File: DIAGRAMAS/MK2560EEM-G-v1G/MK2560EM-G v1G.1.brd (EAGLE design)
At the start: 102.5 x 87.6 mm, 70 parts, among them U1 X-MOTOR, U2 Y-MOTOR, U3 Z-MOTOR

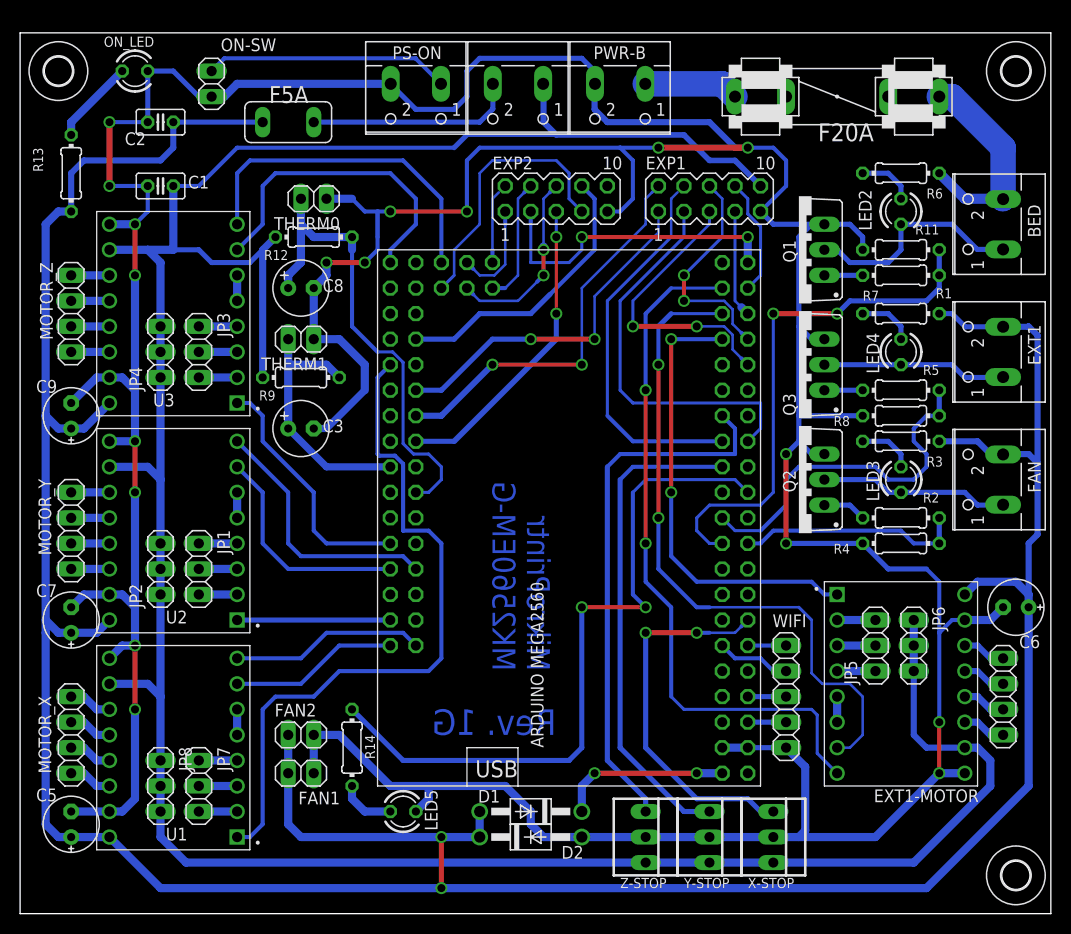
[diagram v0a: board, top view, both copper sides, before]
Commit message: pcb fixes v1G.1
- pcb bug corrections space clearance on x,y,z drivers resolution pin headers. changed for right pin headers.
- changed F5A fuse for +12v rail, for aa short cylinder standard fuse.
- pcb resized, for more space, and better alocation of components.
-
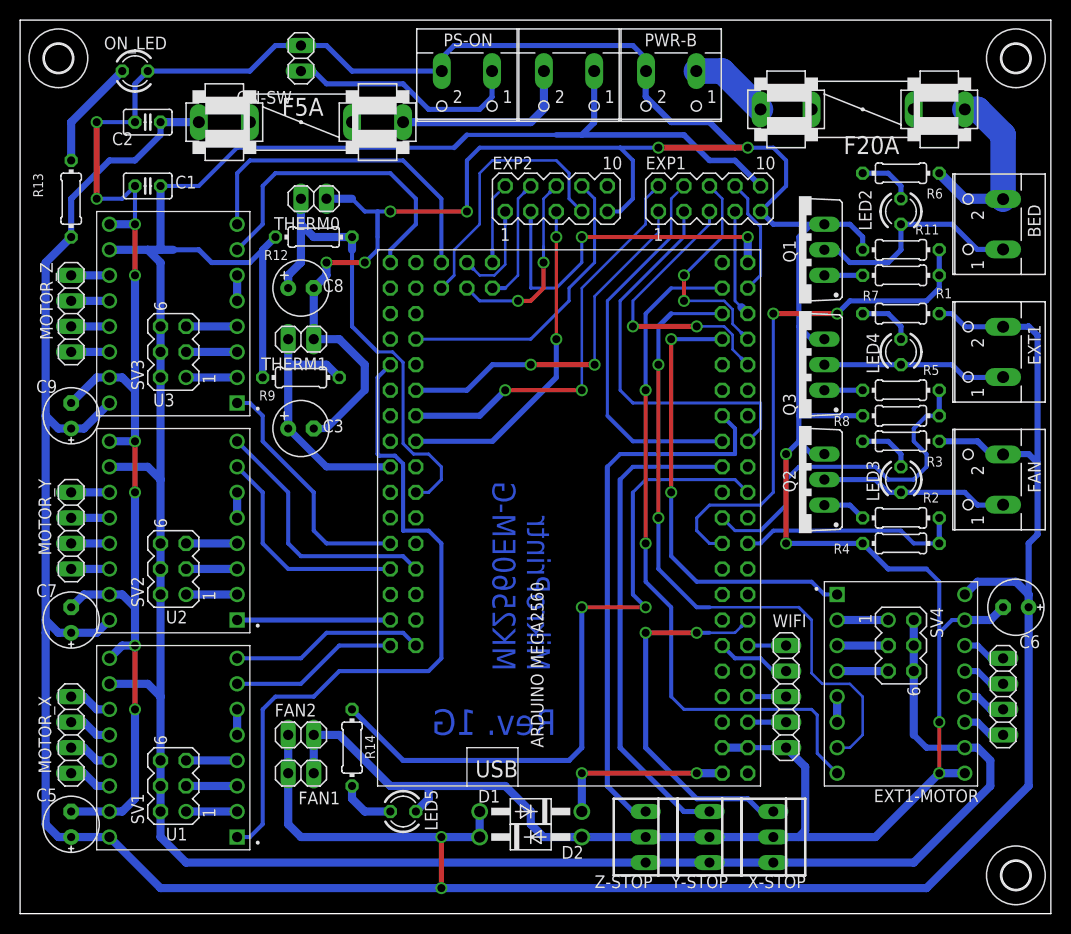
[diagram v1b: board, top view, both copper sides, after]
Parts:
- removed JP1, JP2, JP3, JP4, JP5, JP6, JP7, JP8: (no value), -redpic-connector:1X03
- added SV1, SV2, SV3, SV4: (no value), con-lstb:MA03-2
- F5A: device fuse:TE5 -> special:FUSE1
- moved ON-SW 9.25 mm to (25.4, 76.2), turned to 90 degrees
- moved +12V_+5V 5.24 mm to (52.1, 73.7)
- moved PS-ON 5.24 mm to (41.9, 73.7)
- moved PWR-B 5.24 mm to (62.2, 73.7)
- moved F20A 2.84 mm to (81.3, 71.1)
- moved R13 2.54 mm to (2.54, 62.2)
- moved C1 1.27 mm to (10.2, 63.5)
- moved C2 1.27 mm to (10.2, 69.8)
- moved F5A 1.27 mm to (25.4, 69.8)
- moved H1 1.27 mm to (1.27, 76.2)
- moved H2 1.27 mm to (96.5, 76.2)
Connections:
- net +12V5A: now also F5A.1A; no longer F5A.1
- net +5V: now also SV1.2, SV1.4, SV1.6, SV2.2, SV2.4, SV2.6, SV3.2, SV3.4, SV3.6, SV4.2, SV4.4, SV4.6; no longer JP2.1, JP2.2, JP2.3, JP4.1, JP4.2, JP4.3, JP6.1, JP6.2, JP6.3, JP8.1, JP8.2, JP8.3
- net N$10: now also SV1.3; no longer JP7.2
- net N$11: now also SV1.5; no longer JP7.1
- net N$14: now also SV2.1; no longer JP1.3
- net N$15: now also SV2.3; no longer JP1.2
- net N$16: now also SV2.5; no longer JP1.1
- net N$19: now also SV3.3, U3.3; no longer JP3.3, U3.2
- net N$21: now also SV3.1, U3.2; no longer JP3.2, U3.3
- net N$22: now also SV3.5; no longer JP3.1
- net N$24: now also EXT1-MOTOR.3, SV4.3; no longer EXT1-MOTOR.4, JP5.1
- net N$25: now also EXT1-MOTOR.4, SV4.5; no longer EXT1-MOTOR.3, JP5.2
- net N$26: now also SV4.1; no longer JP5.3
- net N$27: now also F5A.2A; no longer F5A.2
- net N$9: now also SV1.1; no longer JP7.3
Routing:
- net +12V5A: track 351.1 -> 341.8 mm
- net +5V: track 295.6 -> 289.3 mm
- net D31: track 31.0 -> 35.3 mm
- net N$27: track 20.9 -> 18.3 mm
- net N$18: track 8.45 -> 11.0 mm
- net +12V: track 21.0 -> 18.7 mm
- net D33: track 30.9 -> 33.1 mm
- net D35: track 39.6 -> 41.0 mm
- net D41: track 28.3 -> 29.8 mm
- net D37: track 35.2 -> 36.7 mm
- net N$29: track 9.46 -> 7.97 mm
- net N$9: track 3.81 -> 5.08 mm
- net N$22: track 3.81 -> 5.08 mm
- net N$21: track 3.81 -> 5.08 mm
- net N$19: track 3.81 -> 5.08 mm
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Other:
- board size 102.5 x 87.6 mm -> 102.5 x 88.9 mm
